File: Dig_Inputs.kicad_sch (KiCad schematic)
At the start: 32 parts, among them J40 Screw_Terminal_01x02, J6 Screw_Terminal_01x02, U3 LTV-357T

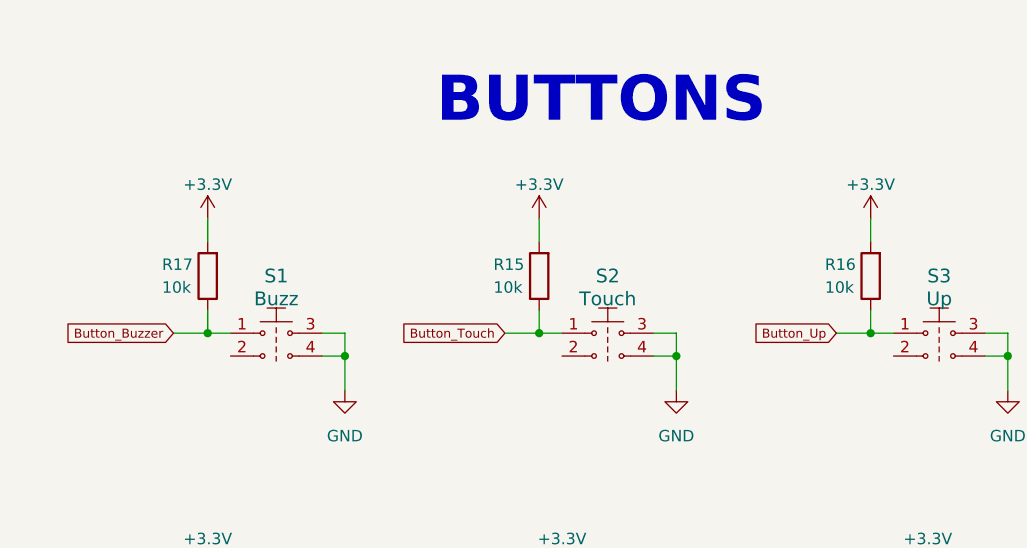
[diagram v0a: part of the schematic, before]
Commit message: SCH: Se cambió el IRM, se colocó filtro en la entrada AC, se modificó la fuente switching LM, se corrigieron algunos errores de diseño. PCB: Se terminó el placement de los componentes
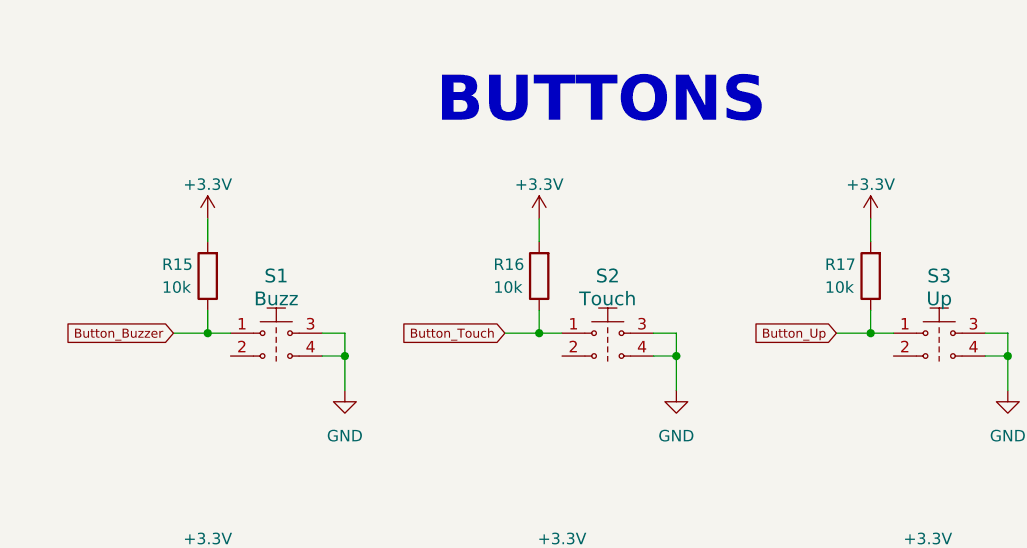
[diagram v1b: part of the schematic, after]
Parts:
- renumbered R17 to R15, R15 to R16, R16 to R17
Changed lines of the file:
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@@
   (symbol (lib_id "1-Resistor:R_0603") (at 173.99 48.26 180) (unit 1)
     (in_bom yes) (on_board yes) (dnp no)
-    (property "Reference" "R17" (at 168.91 46.99 0)
+    (property "Reference" "R15" (at 168.91 46.99 0)
       (effects (font (size 1.27 1.27)) (justify right))
     )
@@
     (instances
       (project "ConsorcioMedico_Refrigeradora"
-        (path "/e86bbed0-5bdc-4982-8297-fb5cecea731c"
-          (reference "R17") (unit 1)
-        )
         (path "/e86bbed0-5bdc-4982-8297-fb5cecea731c/80a96d94-2098-4e0a-a173-fbb6709c7b1a"
           (reference "R15") (unit 1)
@@
     (instances
       (project "ConsorcioMedico_Refrigeradora"
-        (path "/e86bbed0-5bdc-4982-8297-fb5cecea731c"
-          (reference "S3") (unit 1)
-        )
         (path "/e86bbed0-5bdc-4982-8297-fb5cecea731c/80a96d94-2098-4e0a-a173-fbb6709c7b1a"
           (reference "S3") (unit 1)
@@
     (instances
       (project "ConsorcioMedico_Refrigeradora"
-        (path "/e86bbed0-5bdc-4982-8297-fb5cecea731c"
-          (reference "R20") (unit 1)
-        )
         (path "/e86bbed0-5bdc-4982-8297-fb5cecea731c/80a96d94-2098-4e0a-a173-fbb6709c7b1a"
           (reference "R20") (unit 1)
@@
   (symbol (lib_id "1-Resistor:R_0603") (at 247.65 48.26 180) (unit 1)
     (in_bom yes) (on_board yes) (dnp no)
-    (property "Reference" "R16" (at 242.57 46.99 0)
+    (property "Reference" "R17" (at 242.57 46.99 0)
       (effects (font (size 1.27 1.27)) (justify right))
     )
@@
     (instances
       (project "ConsorcioMedico_Refrigeradora"
-        (path "/e86bbed0-5bdc-4982-8297-fb5cecea731c"
-          (reference "R16") (unit 1)
-        )
         (path "/e86bbed0-5bdc-4982-8297-fb5cecea731c/80a96d94-2098-4e0a-a173-fbb6709c7b1a"
           (reference "R17") (unit 1)
@@
       )
       (project "ConsorcioMedico_Refrigeradora"
-        (path "/e86bbed0-5bdc-4982-8297-fb5cecea731c"
-          (reference "#PWR030") (unit 1)
-        )
         (path "/e86bbed0-5bdc-4982-8297-fb5cecea731c/80a96d94-2098-4e0a-a173-fbb6709c7b1a"
           (reference "#PWR030") (unit 1)
@@
     (instances
       (project "ConsorcioMedico_Refrigeradora"
-        (path "/e86bbed0-5bdc-4982-8297-fb5cecea731c"
-          (reference "S1") (unit 1)
-        )
         (path "/e86bbed0-5bdc-4982-8297-fb5cecea731c/80a96d94-2098-4e0a-a173-fbb6709c7b1a"
           (reference "S1") (unit 1)
@@
     (instances
       (project "ConsorcioMedico_Refrigeradora"
-        (path "/e86bbed0-5bdc-4982-8297-fb5cecea731c"
-          (reference "S6") (unit 1)
-        )
         (path "/e86bbed0-5bdc-4982-8297-fb5cecea731c/80a96d94-2098-4e0a-a173-fbb6709c7b1a"
           (reference "S6") (unit 1)
@@
   (symbol (lib_id "power:+12V") (at 29.21 76.2 0) (unit 1)
     (in_bom yes) (on_board yes) (dnp no)
-    (property "Reference" "#PWR085" (at 29.21 80.01 0)
+    (property "Reference" "#PWR086" (at 29.21 80.01 0)
       (effects (font (size 1.27 1.27)) hide)
     )
@@
     (instances
       (project "ConsorcioMedico_Refrigeradora"
-        (path "/e86bbed0-5bdc-4982-8297-fb5cecea731c"
-          (reference "#PWR085") (unit 1)
-        )
         (path "/e86bbed0-5bdc-4982-8297-fb5cecea731c/80a96d94-2098-4e0a-a173-fbb6709c7b1a"
           (reference "#PWR086") (unit 1)
@@
       )
       (project "ConsorcioMedico_Refrigeradora"
-        (path "/e86bbed0-5bdc-4982-8297-fb5cecea731c"
-          (reference "#PWR035") (unit 1)
-        )
         (path "/e86bbed0-5bdc-4982-8297-fb5cecea731c/80a96d94-2098-4e0a-a173-fbb6709c7b1a"
           (reference "#PWR035") (unit 1)
@@
   (symbol (lib_id "power:+12V") (at 26.67 24.13 0) (unit 1)
     (in_bom yes) (on_board yes) (dnp no)
-    (property "Reference" "#PWR085" (at 26.67 27.94 0)
+    (property "Reference" "#PWR037" (at 26.67 27.94 0)
       (effects (font (size 1.27 1.27)) hide)
     )
@@
     (instances
       (project "ConsorcioMedico_Refrigeradora"
-        (path "/e86bbed0-5bdc-4982-8297-fb5cecea731c"
-          (reference "#PWR085") (unit 1)
-        )
         (path "/e86bbed0-5bdc-4982-8297-fb5cecea731c/80a96d94-2098-4e0a-a173-fbb6709c7b1a"
           (reference "#PWR037") (unit 1)
@@
       )
       (project "ConsorcioMedico_Refrigeradora"
-        (path "/e86bbed0-5bdc-4982-8297-fb5cecea731c"
-          (reference "#PWR025") (unit 1)
-        )
         (path "/e86bbed0-5bdc-4982-8297-fb5cecea731c/80a96d94-2098-4e0a-a173-fbb6709c7b1a"
           (reference "#PWR027") (unit 1)
@@
     (instances
       (project "ConsorcioMedico_Refrigeradora"
-        (path "/e86bbed0-5bdc-4982-8297-fb5cecea731c"
-          (reference "S2") (unit 1)
-        )
         (path "/e86bbed0-5bdc-4982-8297-fb5cecea731c/80a96d94-2098-4e0a-a173-fbb6709c7b1a"
           (reference "S2") (unit 1)
@@
       )
       (project "ConsorcioMedico_Refrigeradora"
-        (path "/e86bbed0-5bdc-4982-8297-fb5cecea731c"
-          (reference "#PWR027") (unit 1)
-        )
         (path "/e86bbed0-5bdc-4982-8297-fb5cecea731c/80a96d94-2098-4e0a-a173-fbb6709c7b1a"
           (reference "#PWR028") (unit 1)
@@
     (instances
       (project "ConsorcioMedico_Refrigeradora"
-        (path "/e86bbed0-5bdc-4982-8297-fb5cecea731c"
-          (reference "S4") (unit 1)
-        )
         (path "/e86bbed0-5bdc-4982-8297-fb5cecea731c/80a96d94-2098-4e0a-a173-fbb6709c7b1a"
           (reference "S4") (unit 1)
@@
     (instances
       (project "ConsorcioMedico_Refrigeradora"
-        (path "/e86bbed0-5bdc-4982-8297-fb5cecea731c"
-          (reference "R19") (unit 1)
-        )
         (path "/e86bbed0-5bdc-4982-8297-fb5cecea731c/80a96d94-2098-4e0a-a173-fbb6709c7b1a"
           (reference "R19") (unit 1)
@@
       )
       (project "ConsorcioMedico_Refrigeradora"
-        (path "/e86bbed0-5bdc-4982-8297-fb5cecea731c"
-          (reference "#PWR029") (unit 1)
-        )
         (path "/e86bbed0-5bdc-4982-8297-fb5cecea731c/80a96d94-2098-4e0a-a173-fbb6709c7b1a"
           (reference "#PWR029") (unit 1)
@@
       )
       (project "ConsorcioMedico_Refrigeradora"
-        (path "/e86bbed0-5bdc-4982-8297-fb5cecea731c"
-          (reference "#PWR028") (unit 1)
-        )
         (path "/e86bbed0-5bdc-4982-8297-fb5cecea731c/80a96d94-2098-4e0a-a173-fbb6709c7b1a"
           (reference "#PWR026") (unit 1)
@@
     (instances
       (project "ConsorcioMedico_Refrigeradora"
-        (path "/e86bbed0-5bdc-4982-8297-fb5cecea731c"
-          (reference "S5") (unit 1)
-        )
         (path "/e86bbed0-5bdc-4982-8297-fb5cecea731c/80a96d94-2098-4e0a-a173-fbb6709c7b1a"
           (reference "S5") (unit 1)
@@
       )
       (project "ConsorcioMedico_Refrigeradora"
-        (path "/e86bbed0-5bdc-4982-8297-fb5cecea731c"
-          (reference "#PWR024") (unit 1)
-        )
         (path "/e86bbed0-5bdc-4982-8297-fb5cecea731c/80a96d94-2098-4e0a-a173-fbb6709c7b1a"
           (reference "#PWR025") (unit 1)
@@
       )
       (project "ConsorcioMedico_Refrigeradora"
-        (path "/e86bbed0-5bdc-4982-8297-fb5cecea731c"
-          (reference "#PWR034") (unit 1)
-        )
         (path "/e86bbed0-5bdc-4982-8297-fb5cecea731c/80a96d94-2098-4e0a-a173-fbb6709c7b1a"
           (reference "#PWR032") (unit 1)
@@
       )
       (project "ConsorcioMedico_Refrigeradora"
-        (path "/e86bbed0-5bdc-4982-8297-fb5cecea731c"
-          (reference "#PWR031") (unit 1)
-        )
         (path "/e86bbed0-5bdc-4982-8297-fb5cecea731c/80a96d94-2098-4e0a-a173-fbb6709c7b1a"
           (reference "#PWR033") (unit 1)
@@
       )
       (project "ConsorcioMedico_Refrigeradora"
-        (path "/e86bbed0-5bdc-4982-8297-fb5cecea731c"
-          (reference "#PWR032") (unit 1)
-        )
         (path "/e86bbed0-5bdc-4982-8297-fb5cecea731c/80a96d94-2098-4e0a-a173-fbb6709c7b1a"
           (reference "#PWR031") (unit 1)
@@
       )
       (project "ConsorcioMedico_Refrigeradora"
-        (path "/e86bbed0-5bdc-4982-8297-fb5cecea731c"
-          (reference "#PWR033") (unit 1)
-        )
         (path "/e86bbed0-5bdc-4982-8297-fb5cecea731c/80a96d94-2098-4e0a-a173-fbb6709c7b1a"
           (reference "#PWR034") (unit 1)
@@
     (instances
       (project "ConsorcioMedico_Refrigeradora"
-        (path "/e86bbed0-5bdc-4982-8297-fb5cecea731c"
-          (reference "R18") (unit 1)
-        )
         (path "/e86bbed0-5bdc-4982-8297-fb5cecea731c/80a96d94-2098-4e0a-a173-fbb6709c7b1a"
           (reference "R18") (unit 1)
@@
   (symbol (lib_id "1-Resistor:R_0603") (at 210.82 48.26 180) (unit 1)
     (in_bom yes) (on_board yes) (dnp no)
-    (property "Reference" "R15" (at 205.74 46.99 0)
+    (property "Reference" "R16" (at 205.74 46.99 0)
       (effects (font (size 1.27 1.27)) (justify right))
     )
@@
     (instances
       (project "ConsorcioMedico_Refrigeradora"
-        (path "/e86bbed0-5bdc-4982-8297-fb5cecea731c"
-          (reference "R15") (unit 1)
-        )
         (path "/e86bbed0-5bdc-4982-8297-fb5cecea731c/80a96d94-2098-4e0a-a173-fbb6709c7b1a"
           (reference "R16") (unit 1)
@@
       )
       (project "ConsorcioMedico_Refrigeradora"
-        (path "/e86bbed0-5bdc-4982-8297-fb5cecea731c"
-          (reference "#PWR026") (unit 1)
-        )
         (path "/e86bbed0-5bdc-4982-8297-fb5cecea731c/80a96d94-2098-4e0a-a173-fbb6709c7b1a"
           (reference "#PWR024") (unit 1)

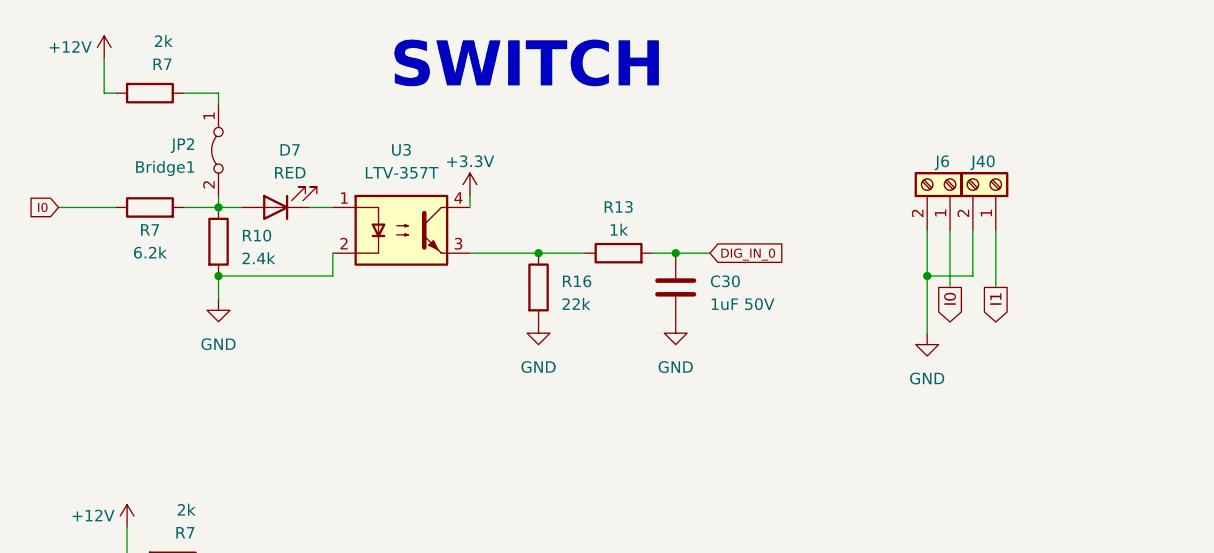
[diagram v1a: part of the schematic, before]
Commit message: SCH: Se modificó la posición de algunos pines para mejorar la calidad del ruteado. PCB: Se enruta las señales, quedando la alimentación, pines de programación, relays y planos de gnd
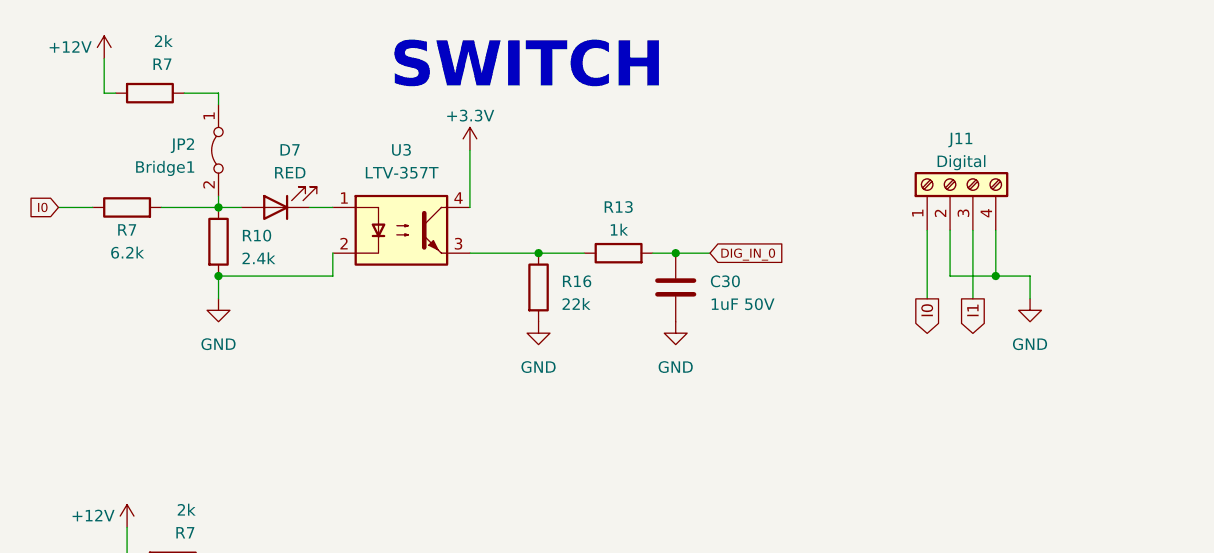
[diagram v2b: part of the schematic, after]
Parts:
- removed J40, J6: Screw_Terminal_01x02, 1-Terminal-Block:DG504-5.08-02P_or_SMKDS 2,5-2-5.08, symbol 1-Terminal-Block:DG504-5.08-02P
- added J11: Digital, 1-Terminal-Block:Terminal-Block_XY2500V-B_4P_P5.0mm_XINYA, symbol Connector:Screw_Terminal_01x04
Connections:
- net GND: now also J11.2 (Pin_2), J11.4 (Pin_4)
- net I0: now also J11.1 (Pin_1)
- net I1: now also J11.3 (Pin_3)
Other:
- moved on the sheet: R7

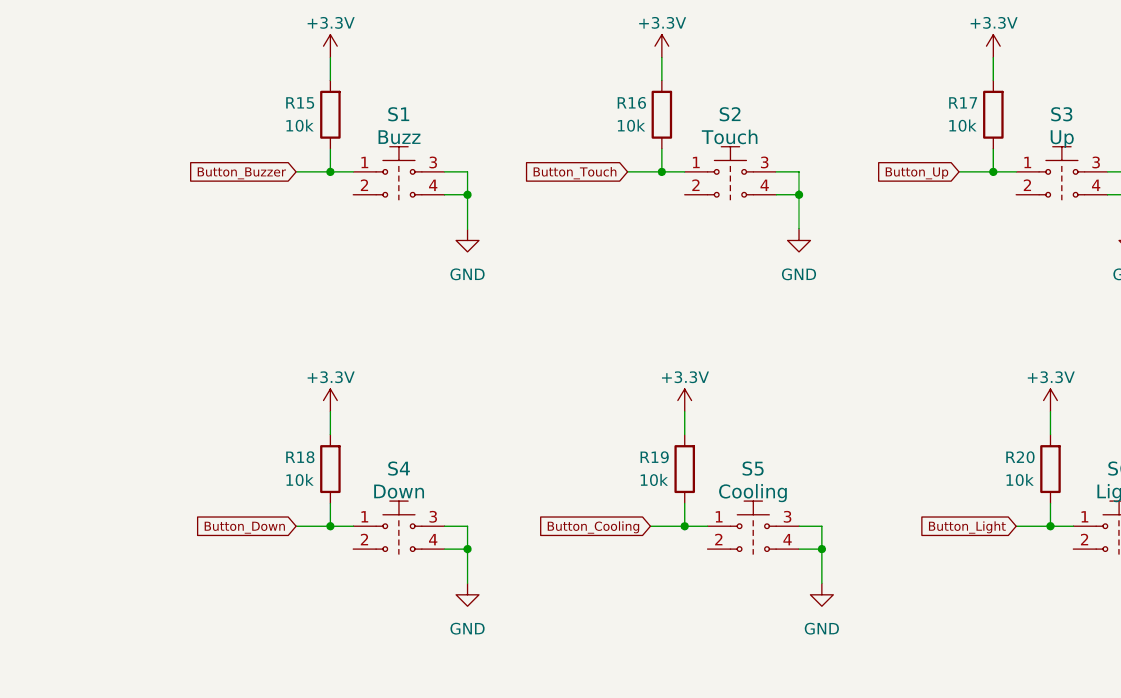
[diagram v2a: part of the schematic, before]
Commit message: SCH: Se arregló la posición de los pulsadores, se agrega buzzer, PCB: Se revisan los componentes y se agrega serigrafía. JLCPCB: Actualizado
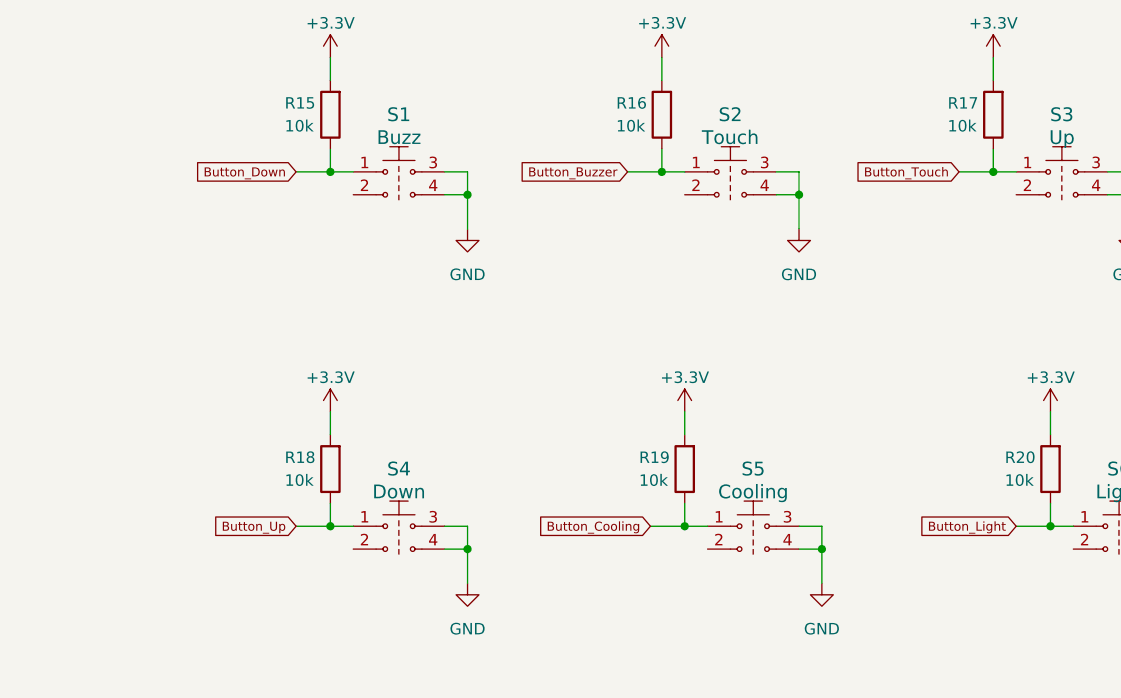
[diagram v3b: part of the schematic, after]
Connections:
- net Button_Buzzer: now also R16.1, S2.1; no longer R15.1, S1.1
- net Button_Down: now also R15.1, S1.1; no longer R18.1, S4.1
- net Button_Touch: now also R17.1, S3.1; no longer R16.1, S2.1
- net Button_Up: now also R18.1, S4.1; no longer R17.1, S3.1
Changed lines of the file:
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@@
-    )
-  )
-  (global_label "Button_Touch" (shape input) (at 207.01 54.61 180) (fields_autoplaced)
-    (effects (font (size 1 1)) (justify right))
-    (property "Intersheetrefs" "${INTERSHEET_REFS}" (at 194.7696 54.61 0)
-      (effects (font (size 1.27 1.27)) (justify right) hide)
     )
   )
@@
     (effects (font (size 1 1)) (justify right))
     (property "Intersheetrefs" "${INTERSHEET_REFS}" (at 25.4935 92.71 0)
-      (effects (font (size 1.27 1.27)) (justify right) hide)
-    )
-  )
-  (global_label "Button_Down" (shape input) (at 170.18 93.98 180) (fields_autoplaced)
-    (effects (font (size 1 1)) (justify right))
-    (property "Intersheetrefs" "${INTERSHEET_REFS}" (at 158.4158 93.98 0)
-      (effects (font (size 1.27 1.27)) (justify right) hide)
-    )
-  )
-  (global_label "Button_Up" (shape input) (at 243.84 54.61 180) (fields_autoplaced)
-    (effects (font (size 1 1)) (justify right))
-    (property "Intersheetrefs" "${INTERSHEET_REFS}" (at 233.9806 54.61 0)
       (effects (font (size 1.27 1.27)) (justify right) hide)
     )
@@
     )
   )
-  (global_label "Button_Buzzer" (shape input) (at 170.18 54.61 180) (fields_autoplaced)
+  (global_label "Button_Touch" (shape input) (at 243.84 54.61 180) (fields_autoplaced)
     (effects (font (size 1 1)) (justify right))
-    (property "Intersheetrefs" "${INTERSHEET_REFS}" (at 157.2731 54.61 0)
+    (property "Intersheetrefs" "${INTERSHEET_REFS}" (at 231.5996 54.61 0)
+      (effects (font (size 1.27 1.27)) (justify right) hide)
+    )
+  )
+  (global_label "Button_Down" (shape input) (at 170.18 54.61 180) (fields_autoplaced)
+    (effects (font (size 1 1)) (justify right))
+    (property "Intersheetrefs" "${INTERSHEET_REFS}" (at 158.4158 54.61 0)
+      (effects (font (size 1.27 1.27)) (justify right) hide)
+    )
+  )
+  (global_label "Button_Buzzer" (shape input) (at 207.01 54.61 180) (fields_autoplaced)
+    (effects (font (size 1 1)) (justify right))
+    (property "Intersheetrefs" "${INTERSHEET_REFS}" (at 194.1031 54.61 0)
       (effects (font (size 1.27 1.27)) (justify right) hide)
     )
@@
       (effects (font (size 1.27 1.27)) (justify right) hide)
     )
+  )
+  (global_label "Button_Up" (shape input) (at 170.18 93.98 180) (fields_autoplaced)
+    (effects (font (size 1 1)) (justify right))
+    (property "Intersheetrefs" "${INTERSHEET_REFS}" (at 160.3206 93.98 0)
+      (effects (font (size 1.27 1.27)) (justify right) hide)
+    )
